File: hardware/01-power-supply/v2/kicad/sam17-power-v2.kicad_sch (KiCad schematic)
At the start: 54 parts, among them J1 12VAC CT 2A, J2 BUS +12/G/G/-12, J3 AC 230V IN, J4 TR1 pri (ext), J5 CHASIS, J6 +5V/RTN, J7 SMPS 230V TAP, Q1 BT169D, U1 LM2941CT/NOPB, U2 LM2991T/NOPB, U3 LM7805

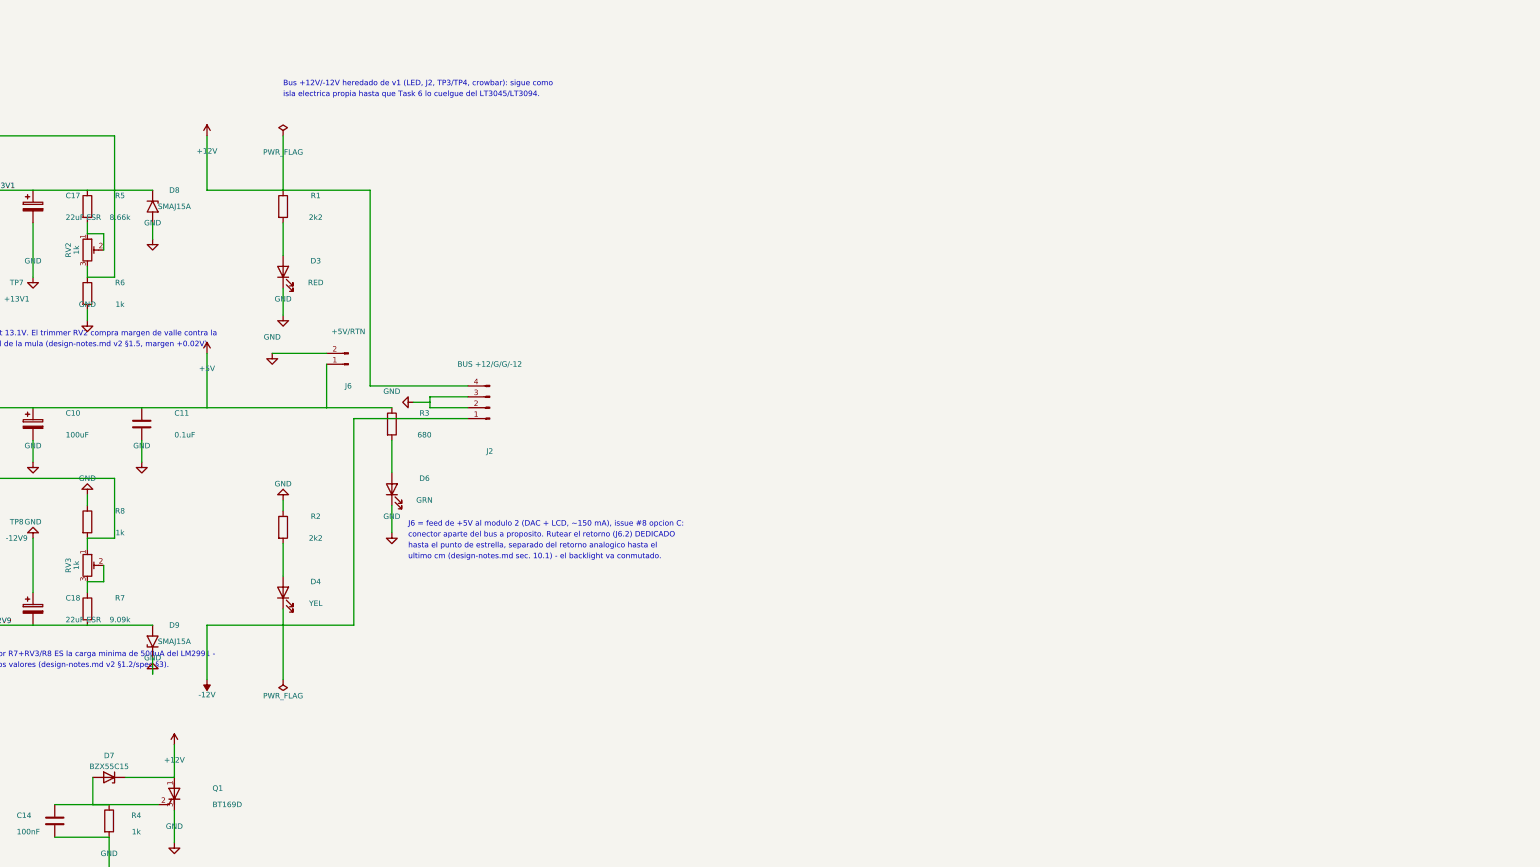
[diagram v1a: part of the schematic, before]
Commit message: Esquematico v2 completo: LT3045/LT3094 en paralelo con SET compartida e isla GNDREF
Etapa ultra sobre simbolos estandar (Regulator_Linear:LT3045xDD/LT3094xDD,
sin simbolo local): U4/U5 en paralelo sobre +13V1->+12V, U6/U7 en paralelo
sobre -12V9->-12V, SET compartido por riel (R9/C15, R10/C16) a GNDREF, ILIM
por chip (R11-R14) con Kelvin a la masa propia, ballast 20mOhm (R15-R18),
Schottkys D10/D11 (D11 espejo negativo de D10, mismo patron que D12/D13),
JP1 como unico puente GNDREF<->GND. Divisores de U1/U2 (R6/R8) movidos de
GND a GNDREF. Isla +12V/-12V heredada de v1 reconectada de verdad al
ballast/OUTS. Hoja a A2 (hacia falta mas ancho).

check_bom.py: OK cuadre total (0/0/0, 81 en hoja == 88 en BOM menos
TR/HS/XU fuera de hoja). ERC via kicad-cli --severity-error: 0 violaciones.
Netlist exportado y verificado nodo a nodo: EP(LT3045)=GND, EP(LT3094)=IN,
GNDREF aislada (5 nodos, solo JP1 la toca), OUTS a nodo real, PG/PGFB/VIOC
flotantes via no_connect explicito.

Bug real cazado por el propio assert de pines del script: X_D (ancla de
D10/D11) caia fuera de la rejilla de 1.27mm, el MCP lo redondeaba en
colocacion sin avisar y las wires (calculadas contra el valor sin redondear)
quedaban 0.63mm desalineadas -- documentado en task-6-report.md.

Co-Authored-By: Claude Fable 5 <noreply@anthropic.com>
Claude-Session: https://claude.ai/code/session_01Xqa4XDcufx4ptQE2gEAZoo
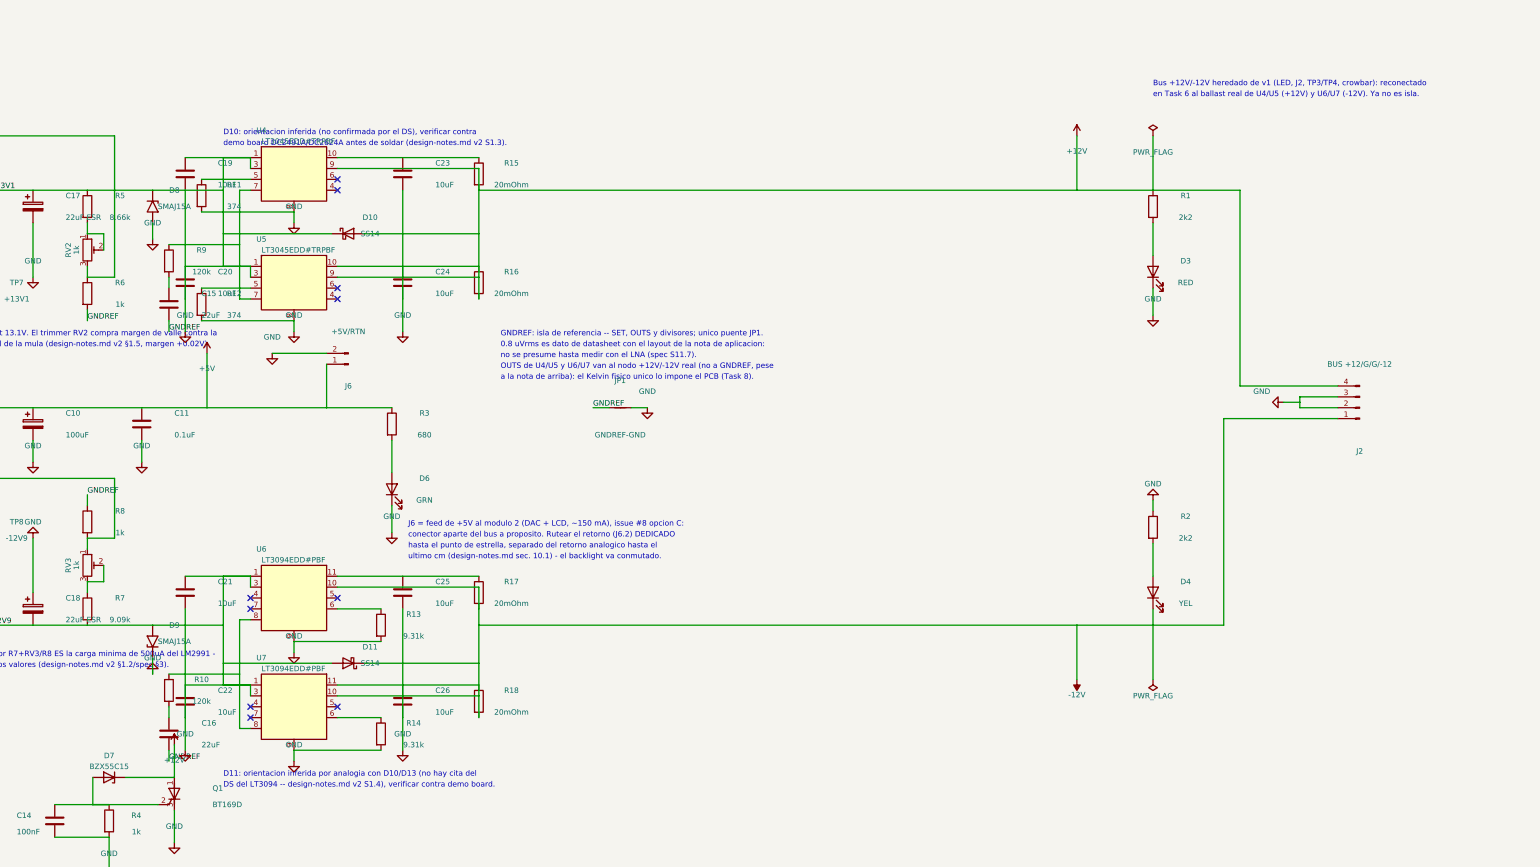
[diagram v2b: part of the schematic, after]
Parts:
- added C15, C16: 22uF, Capacitor_SMD:C_1210_3225Metric, symbol Device:C
- added C19, C20, C21, C22, C23, C24, C25, C26: 10uF, Capacitor_SMD:C_1206_3216Metric, symbol Device:C
- added D10, D11: SS14, Diode_SMD:D_SMA, symbol Diode:SS14
- added JP1: GNDREF-GND, NetTie:NetTie-2_SMD_Pad0.5mm, symbol Device:NetTie_2
- added R10, R9: 120k, Resistor_SMD:R_0805_2012Metric, symbol Device:R
- added R11, R12: 374, Resistor_SMD:R_0603_1608Metric, symbol Device:R
- added R13, R14: 9.31k, Resistor_SMD:R_0603_1608Metric, symbol Device:R
- added R15, R16, R17, R18: 20mOhm, Resistor_SMD:R_1206_3216Metric, symbol Device:R
- added U4, U5: LT3045EDD#TRPBF, Package_DFN_QFN:DFN-10-1EP_3x3mm_P0.5mm_EP1.65x2.38mm, symbol Regulator_Linear:LT3045xDD
- added U6, U7: LT3094EDD#PBF, Package_DFN_QFN:DFN-12-1EP_3x3mm_P0.45mm_EP1.65x2.38mm_ThermalVias, symbol Regulator_Linear:LT3094xDD
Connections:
- net +12V: now also D10.2 (A), R15.2, R16.2, U4.9 (OUTS), U5.9 (OUTS)
- net +13V1: now also C19.1, C20.1, D10.1 (K), U4.1 (IN), U4.2 (IN), U4.3 (EN/UV), U5.1 (IN), U5.2 (IN), U5.3 (EN/UV)
- net -12V: now also D11.1 (K), R17.2, R18.2, U6.10 (OUTS), U7.10 (OUTS)
- net -12V9: now also C21.1, C22.1, D11.2 (A), U6.1 (IN), U6.13 (IN), U6.2 (IN), U6.3 (EN/UV), U7.1 (IN), U7.13 (IN), U7.2 (IN), U7.3 (EN/UV)
- net GND: now also C19.2, C20.2, C21.2, C22.2, C23.2, C24.2, C25.2, C26.2, JP1.2, R11.2, R12.2, R13.2, R14.2, U4.11 (GND), U4.8 (GND), U5.11 (GND), U5.8 (GND), U6.9 (GND), U7.9 (GND); no longer R6.2, R8.1
- new net: C26.1, R18.1, U7.11 (OUT), U7.12 (OUT)
- new net: R13.1, U6.6 (ILIM)
- new net: R9.1, U4.7 (SET), U5.7 (SET)
- new net: C15.1, R9.2
- new net: C23.1, R15.1, U4.10 (OUT)
- new net: R11.1, U4.5 (ILIM)
- new net: R14.1, U7.6 (ILIM)
- new net: C24.1, R16.1, U5.10 (OUT)
- new net: C25.1, R17.1, U6.11 (OUT), U6.12 (OUT)
- new net: R12.1, U5.5 (ILIM)
- new net: C16.1, R10.2
- new net: R10.1, U6.8 (SET), U7.8 (SET)
- new net GNDREF: C15.2, C16.2, JP1.1, R6.2, R8.1
- no-connect marks 0 -> 10
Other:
- note added: "0.8 uVrms es dato de datasheet con el layout de la nota de aplicacion:"
- note added: "Bus +12V/-12V heredado de v1 (LED, J2, TP3/TP4, crowbar): reconectado"
- note added: "D10: orientacion inferida (no confirmada por el DS), verificar contra"
- note added: "D11: orientacion inferida por analogia con D10/D13 (no hay cita del"
- note added: "DS del LT3094 -- design-notes.md v2 S1.4), verificar contra demo board."
- note added: "GNDREF: isla de referencia -- SET, OUTS y divisores; unico puente JP1."
- note added: "OUTS de U4/U5 y U6/U7 van al nodo +12V/-12V real (no a GNDREF, pese"
- note added: "a la nota de arriba): el Kelvin fisico unico lo impone el PCB (Task 8)."
- note added: "demo board DC2491A/DC2624A antes de soldar (design-notes.md v2 S1.3)."
- note added: "en Task 6 al ballast real de U4/U5 (+12V) y U6/U7 (-12V). Ya no es isla."
- note added: "no se presume hasta medir con el LNA (spec S11.7)."
- note removed: "Bus +12V/-12V heredado de v1 (LED, J2, TP3/TP4, crowbar): sigue como"
- note removed: "isla electrica propia hasta que Task 6 lo cuelgue del LT3045/LT3094."

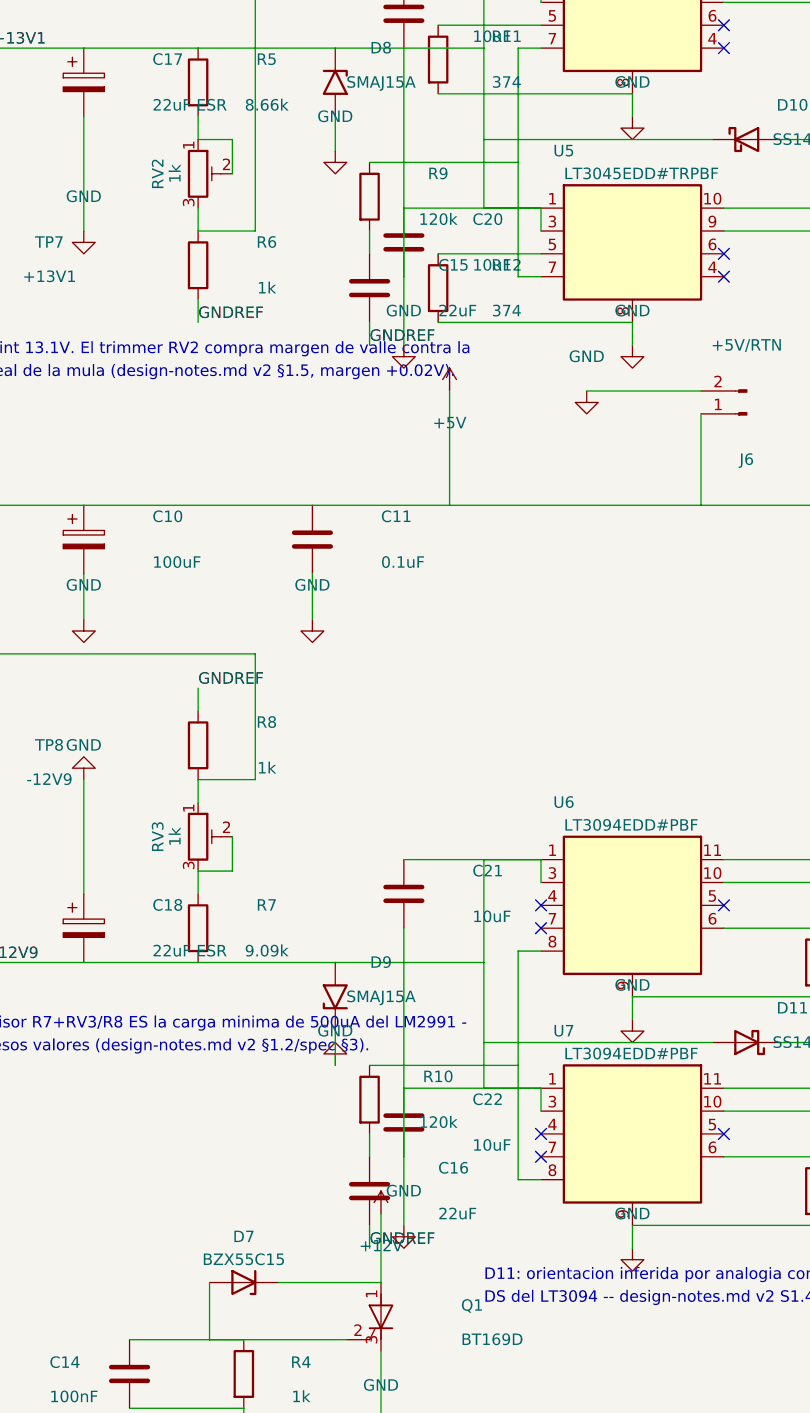
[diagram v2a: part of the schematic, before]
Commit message: Fix round 1 Task 6: R9/C15 y R10/C16 en paralelo (estaban en serie)
CRITICAL del task review: el wire "R9->C15 gap" unia la pata inferior de
R9 con la superior de C15 -- SET->R9->nodo->C15->GNDREF en serie, lo que
le corta a I_SET (100uA, pin SET) el camino DC a masa (el cap bloquea DC).
Los 4 chips no habrian regulado.

Fix: nueva columna X_RCSET2=238.76 (sin colision con las wires ADJ U1/ADJ
U2 en x=232.41, verificado antes de mover nada), C15/C16 al lado de R9/R10
(mismo Y de ancla, ya no apiladas una encima de la otra) y taps via rail()
de 2/3 puntos en vez del wire serie. Espejo identico para R10/C16.

Verificado yo mismo en el netlist exportado, no de memoria: R9.1/C15.1 y
R10.1/C16.1 en el net SET compartido de cada pareja; R9.2/C15.2 y
R10.2/C16.2 en GNDREF. Red GNDREF sigue aislada (7 nodos, solo JP1 la toca).

check_bom.py: OK cuadre total. ERC via kicad-cli --severity-error: 0
violaciones.

Co-Authored-By: Claude Fable 5 <noreply@anthropic.com>
Claude-Session: https://claude.ai/code/session_01Xqa4XDcufx4ptQE2gEAZoo
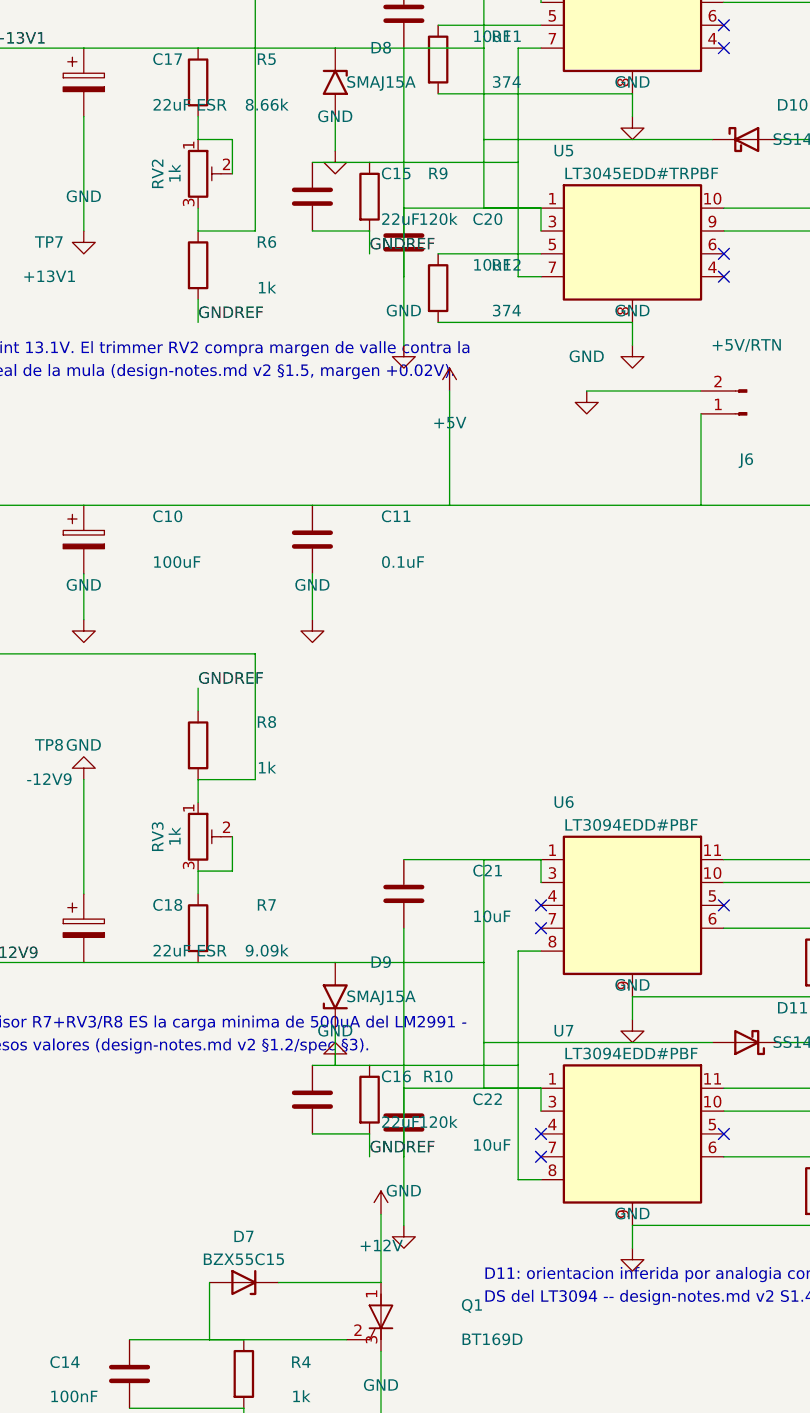
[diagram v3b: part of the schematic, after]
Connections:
- net GNDREF: now also R10.2, R9.2
- net at R9.1, U4.7 (SET), U5.7 (SET): now also C15.1
- net at C16.1: now also R10.1, U6.8 (SET), U7.8 (SET); no longer R10.2

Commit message: fix(hw/psu-v2): U6/U7 sin footprint _ThermalVias (0.2mm viola JLC/placa)
El footprint DFN-12-1EP..._ThermalVias trae vias de 0.2mm de taladro en
el propio pad del EP, por debajo del minimo de fabricacion JLC de 2
capas (0.3mm) y de las reglas de la placa. Cambio a la variante sin
vias (EP1.65x2.38mm, sin sufijo) en bom.csv y build_schematic.py; la
conexion del EP a -12V9 se resuelve ahora con una via farm manual de
0.3mm en build_pcb.py, igual que el patron de GND de U4/U5.

Esquematico regenerado desde build_schematic.py (ERC: 0 errores).

Co-Authored-By: Claude Fable 5 <noreply@anthropic.com>
Claude-Session: https://claude.ai/code/session_01Xqa4XDcufx4ptQE2gEAZoo
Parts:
- U6, U7: footprint Package_DFN_QFN:DFN-12-1EP_3x3mm_P0.45mm_EP1.65x2.38mm_ThermalVias -> Package_DFN_QFN:DFN-12-1EP_3x3mm_P0.45mm_EP1.65x2.38mm

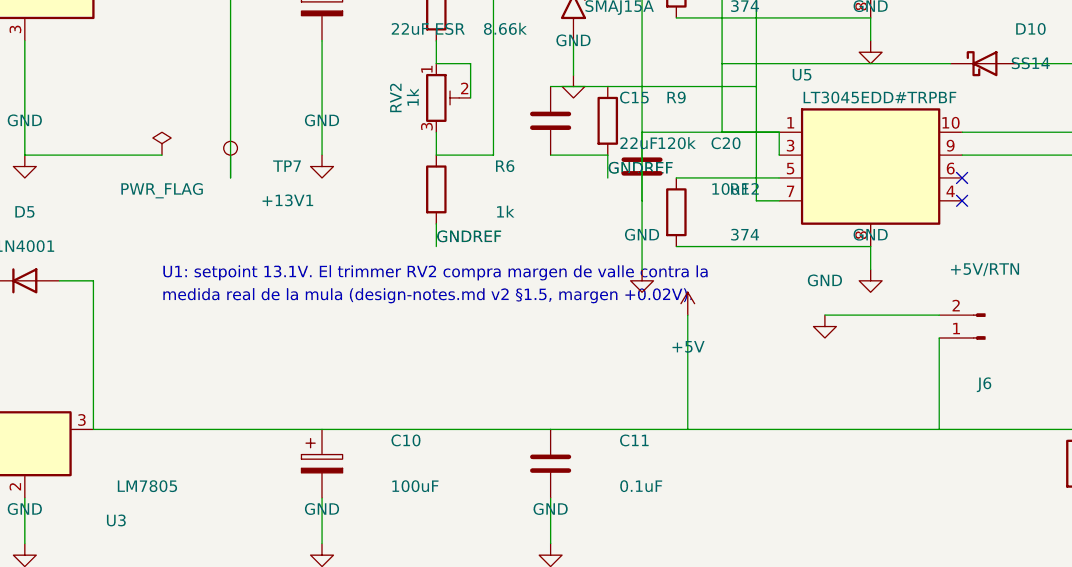
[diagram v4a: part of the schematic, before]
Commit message: La v1 no se construye: la v2 se ajusta contra sus propias medidas
La v1 era la mula contra la que se iban a congelar los setpoints antes de
fabricar la v2. Se cancela: se va directo a la v2 y RV2/RV3 se ajustan en
sitio durante el bring-up. Eso quita la puerta que bloqueaba el pedido y
deja las dos que quedan (stock LCSC, rotaciones de DFN) dentro del propio
flujo del pedido.

Lo que la decision mete en la mesa de pruebas, y por eso es lo mas
importante de este commit: notes v2 §4.1 calcula el UMBRAL DE ABORTO
encadenando los dropouts garantizados de §1.5 y §1.5.1 --

  valle_min = 12.000 (Vout) + dropout_max(LT) + ballast + dropout_max(pre-reg)
  positivo: 12.000 + 0.450 + 0.007 + 1.000 = 13.457 V  <- manda
  negativo: 12.000 + 0.410 + 0.007 + 1.000 = 13.417 V

13.46 V contra un valle simulado de 14.12 V => 0.66 V de colchon. Ese
colchon es exactamente lo que se compra saltandose la mula: el valle real
puede salir 4.7% por debajo del simulado y el trimmer todavia la salva.
Por debajo, ningun setpoint funciona. El paso 5 del bring-up (§5) ahora
para ahi en vez de seguir.

Tambien: se espera BAJAR RV2 a ~12.9 V en el bring-up, porque el setpoint
nominal de 13.1 V solo tiene +0.02 V de margen. No es un fallo, es el
primer ajuste previsto. La nota del esquematico junto a U1 pasa a decir
eso y el umbral, en vez de mandar a medir una mula que no existe.

Fila 3 de §4 (comparativa de rizado v1/v2) anulada: necesitaba una v1
fisica.

--- bug encontrado al regenerar (estaba en main) ---

sym-lib-table tenia la uri de sam17.kicad_sym como ruta ABSOLUTA al
worktree de la ejecucion SDD (.claude/worktrees/psu-v2/...), ya borrado.
Y register_symbol_library es idempotente-por-nombre: contesta
already_registered=True y no reescribe. Resultado en cualquier otra ruta:
la libreria no resuelve, add_schematic_component falla EN SILENCIO para
U1/U2, y build_schematic.py regenera un esquematico SIN los dos
pre-reguladores -- ERC de 0 a 2 errores, .kicad_sch 508 lineas mas corto.
Es decir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
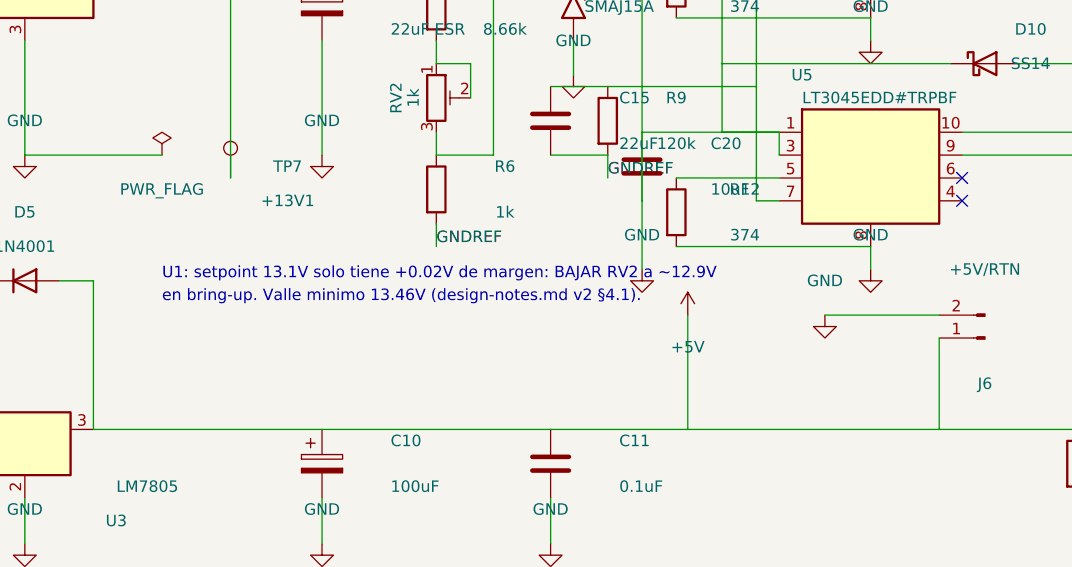
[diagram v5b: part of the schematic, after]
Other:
- note added: "U1: setpoint 13.1V solo tiene +0.02V de margen: BAJAR RV2 a ~12.9V"
- note added: "en bring-up. Valle minimo 13.46V (design-notes.md v2 §4.1)."
- note removed: "U1: setpoint 13.1V. El trimmer RV2 compra margen de valle contra la"
- note removed: "medida real de la mula (design-notes.md v2 §1.5, margen +0.02V)."
